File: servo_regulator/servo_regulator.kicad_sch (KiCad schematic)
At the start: 18 parts, among them J1 Conn_01x03_Socket, Q1 2N7002K

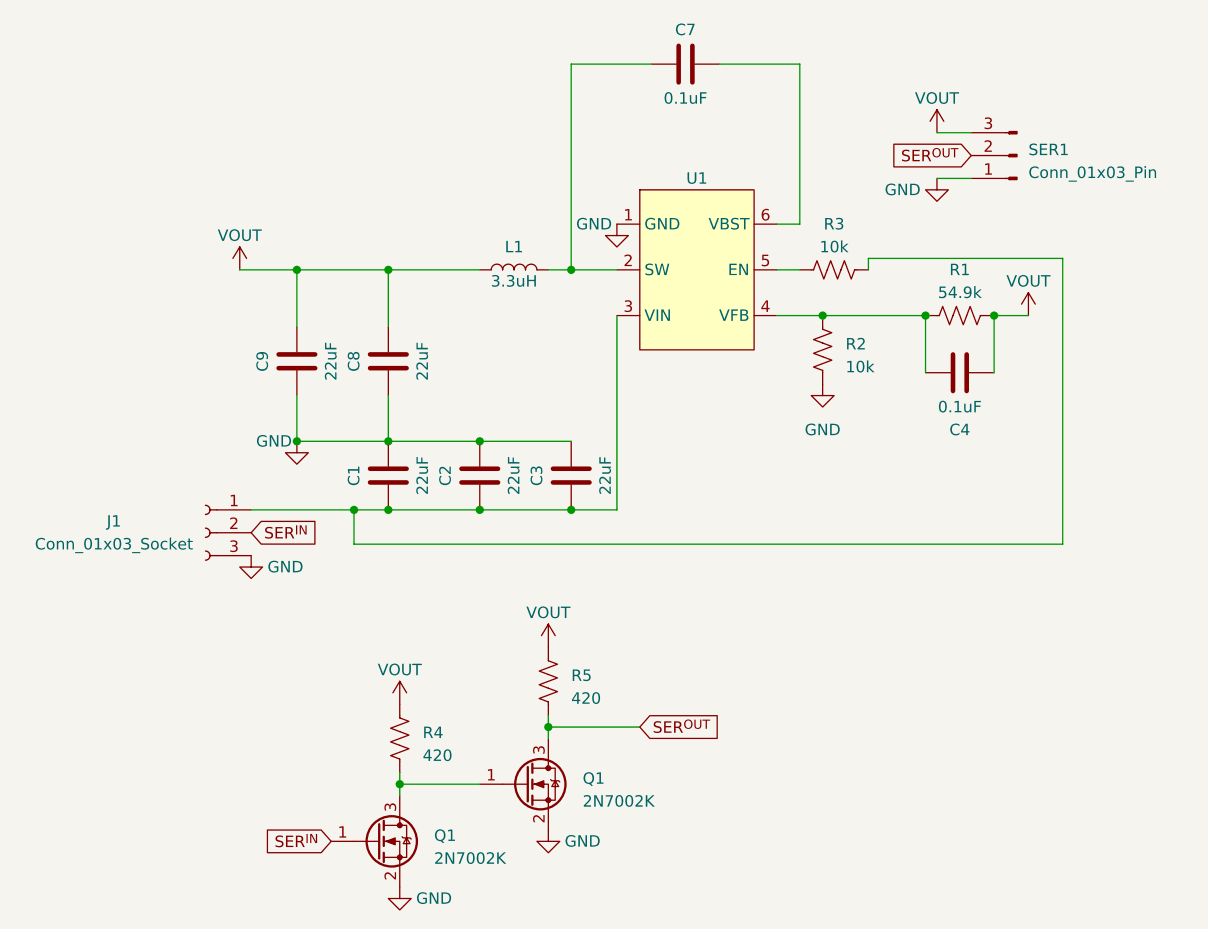
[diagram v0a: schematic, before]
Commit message: Updated spar sensor to reflect order
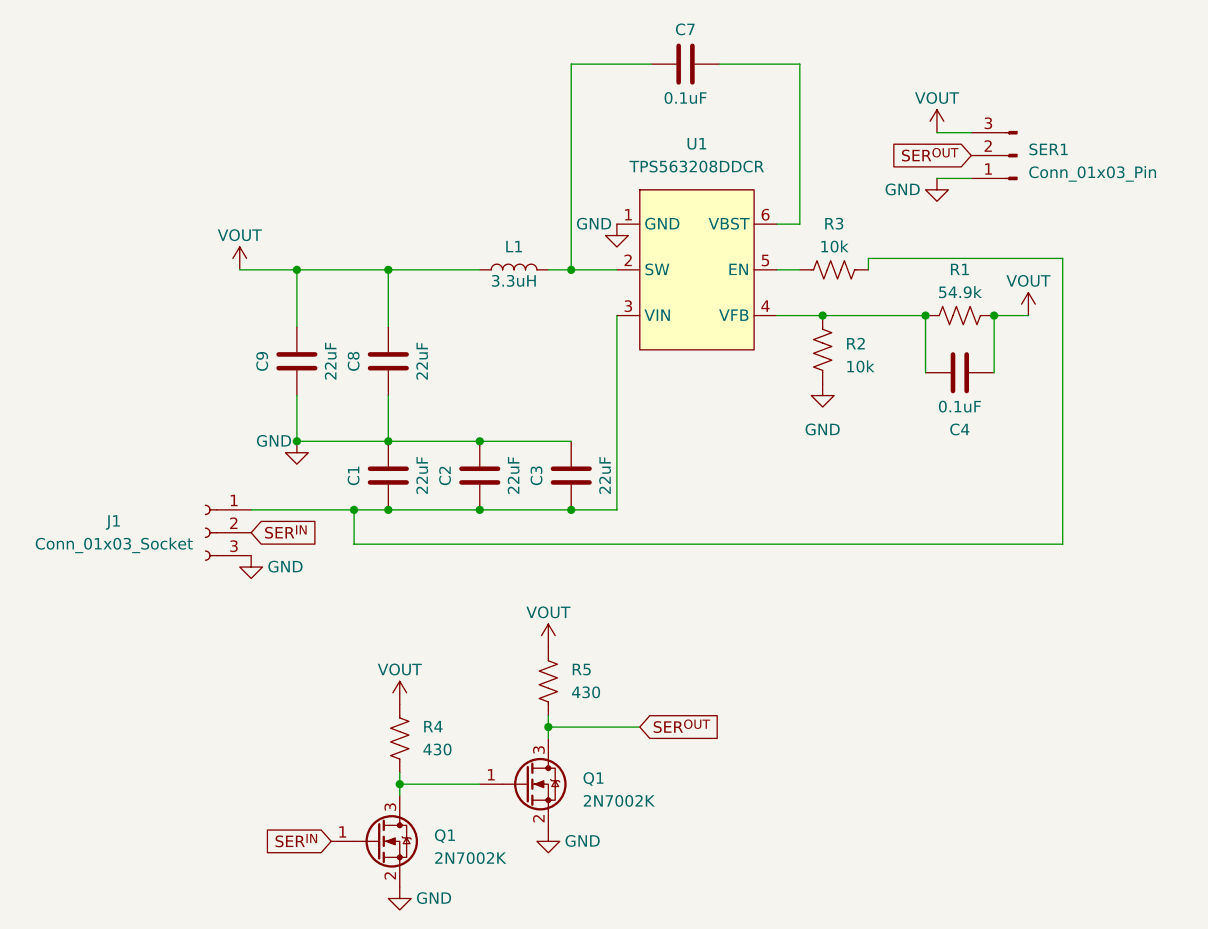
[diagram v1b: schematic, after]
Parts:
- R4, R5: value 420 -> 430
- U1: value ~ -> TPS563208DDCR
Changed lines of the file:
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@@
     (pin "2")
     (instances
-      (project "servoregulatorsv1"
+      (project "servo_regulator"
         (path "/73a2c705-23c6-4b38-b747-fa1f3c1277cb"
           (reference "R3") (unit 1)
@@
     (pin "1")
     (instances
-      (project "servoregulatorsv1"
+      (project "servo_regulator"
         (path "/73a2c705-23c6-4b38-b747-fa1f3c1277cb"
           (reference "#PWR01") (unit 1)
@@
     (pin "1")
     (instances
-      (project "servoregulatorsv1"
+      (project "servo_regulator"
         (path "/73a2c705-23c6-4b38-b747-fa1f3c1277cb"
           (reference "#PWR05") (unit 1)
@@
   (symbol (lib_id "Device:R_US") (at 125.73 137.16 0) (unit 1)
     (in_bom yes) (on_board yes) (dnp no) (fields_autoplaced)
-    (property "Reference" "R5" (at 128.27 136.525 0)
+    (property "Reference" "R5" (at 128.27 135.89 0)
       (effects (font (size 1.27 1.27)) (justify left))
     )
-    (property "Value" "420" (at 128.27 139.065 0)
+    (property "Value" "430" (at 128.27 138.43 0)
       (effects (font (size 1.27 1.27)) (justify left))
     )
@@
     (pin "2")
     (instances
-      (project "servoregulatorsv1"
+      (project "servo_regulator"
         (path "/73a2c705-23c6-4b38-b747-fa1f3c1277cb"
           (reference "R5") (unit 1)
@@
   (symbol (lib_id "Regulators:TPS563208DDCR") (at 142.24 91.44 0) (unit 1)
     (in_bom yes) (on_board yes) (dnp no) (fields_autoplaced)
-    (property "Reference" "U1" (at 142.24 81.28 0)
-      (effects (font (size 1.27 1.27)))
-    )
-    (property "Value" "~" (at 123.19 102.87 0)
+    (property "Reference" "U1" (at 142.24 77.47 0)
+      (effects (font (size 1.27 1.27)))
+    )
+    (property "Value" "TPS563208DDCR" (at 142.24 80.01 0)
       (effects (font (size 1.27 1.27)))
     )
@@
     (pin "6")
     (instances
-      (project "servoregulatorsv1"
+      (project "servo_regulator"
         (path "/73a2c705-23c6-4b38-b747-fa1f3c1277cb"
           (reference "U1") (unit 1)
@@
         )
       )
-      (project "servoregulatorsv1"
+      (project "servo_regulator"
         (path "/73a2c705-23c6-4b38-b747-fa1f3c1277cb"
           (reference "Q1") (unit 1)
@@
     (pin "1")
     (instances
-      (project "servoregulatorsv1"
+      (project "servo_regulator"
         (path "/73a2c705-23c6-4b38-b747-fa1f3c1277cb"
           (reference "#PWR07") (unit 1)
@@
     (pin "1")
     (instances
-      (project "servoregulatorsv1"
+      (project "servo_regulator"
         (path "/73a2c705-23c6-4b38-b747-fa1f3c1277cb"
           (reference "#PWR08") (unit 1)
@@
     (pin "2")
     (instances
-      (project "servoregulatorsv1"
+      (project "servo_regulator"
         (path "/73a2c705-23c6-4b38-b747-fa1f3c1277cb"
           (reference "C7") (unit 1)
@@
     (pin "2")
     (instances
-      (project "servoregulatorsv1"
+      (project "servo_regulator"
         (path "/73a2c705-23c6-4b38-b747-fa1f3c1277cb"
           (reference "L1") (unit 1)
@@
     (pin "1")
     (instances
-      (project "servoregulatorsv1"
+      (project "servo_regulator"
         (path "/73a2c705-23c6-4b38-b747-fa1f3c1277cb"
           (reference "#PWR09") (unit 1)
@@
     (pin "1")
     (instances
-      (project "servoregulatorsv1"
+      (project "servo_regulator"
         (path "/73a2c705-23c6-4b38-b747-fa1f3c1277cb"
           (reference "#PWR03") (unit 1)
@@
     (pin "1")
     (instances
-      (project "servoregulatorsv1"
+      (project "servo_regulator"
         (path "/73a2c705-23c6-4b38-b747-fa1f3c1277cb"
           (reference "#PWR011") (unit 1)
@@
     (pin "1")
     (instances
-      (project "servoregulatorsv1"
+      (project "servo_regulator"
         (path "/73a2c705-23c6-4b38-b747-fa1f3c1277cb"
           (reference "#PWR010") (unit 1)
@@
     (pin "3")
     (instances
-      (project "servoregulatorsv1"
+      (project "servo_regulator"
         (path "/73a2c705-23c6-4b38-b747-fa1f3c1277cb"
           (reference "SER1") (unit 1)
@@
     (pin "2")
     (instances
-      (project "servoregulatorsv1"
+      (project "servo_regulator"
         (path "/73a2c705-23c6-4b38-b747-fa1f3c1277cb"
           (reference "C3") (unit 1)
@@
     (pin "1")
     (instances
-      (project "servoregulatorsv1"
+      (project "servo_regulator"
         (path "/73a2c705-23c6-4b38-b747-fa1f3c1277cb"
           (reference "#PWR06") (unit 1)
@@
     (pin "1")
     (instances
-      (project "servoregulatorsv1"
+      (project "servo_regulator"
         (path "/73a2c705-23c6-4b38-b747-fa1f3c1277cb"
           (reference "#PWR04") (unit 1)
@@
     (pin "2")
     (instances
-      (project "servoregulatorsv1"
+      (project "servo_regulator"
         (path "/73a2c705-23c6-4b38-b747-fa1f3c1277cb"
           (reference "C9") (unit 1)
@@
     (pin "2")
     (instances
-      (project "servoregulatorsv1"
+      (project "servo_regulator"
         (path "/73a2c705-23c6-4b38-b747-fa1f3c1277cb"
           (reference "C8") (unit 1)
@@
     (pin "2")
     (instances
-      (project "servoregulatorsv1"
+      (project "servo_regulator"
         (path "/73a2c705-23c6-4b38-b747-fa1f3c1277cb"
           (reference "C4") (unit 1)
@@
     (pin "1")
     (instances
-      (project "servoregulatorsv1"
+      (project "servo_regulator"
         (path "/73a2c705-23c6-4b38-b747-fa1f3c1277cb"
           (reference "#PWR02") (unit 1)
@@
     (pin "2")
     (instances
-      (project "servoregulatorsv1"
+      (project "servo_regulator"
         (path "/73a2c705-23c6-4b38-b747-fa1f3c1277cb"
           (reference "C2") (unit 1)
@@
     (pin "3")
     (instances
-      (project "servoregulatorsv1"
+      (project "servo_regulator"
         (path "/73a2c705-23c6-4b38-b747-fa1f3c1277cb"
           (reference "J1") (unit 1)
@@
     (pin "2")
     (instances
-      (project "servoregulatorsv1"
+      (project "servo_regulator"
         (path "/73a2c705-23c6-4b38-b747-fa1f3c1277cb"
           (reference "R1") (unit 1)
@@
     (pin "2")
     (instances
-      (project "servoregulatorsv1"
+      (project "servo_regulator"
         (path "/73a2c705-23c6-4b38-b747-fa1f3c1277cb"
           (reference "C1") (unit 1)
@@
     (pin "1")
     (instances
-      (project "servoregulatorsv1"
+      (project "servo_regulator"
         (path "/73a2c705-23c6-4b38-b747-fa1f3c1277cb"
           (reference "#PWR012") (unit 1)
@@
         )
       )
-      (project "servoregulatorsv1"
+      (project "servo_regulator"
         (path "/73a2c705-23c6-4b38-b747-fa1f3c1277cb"
           (reference "Q2") (unit 1)
@@
   (symbol (lib_id "Device:R_US") (at 109.22 143.51 0) (unit 1)
     (in_bom yes) (on_board yes) (dnp no) (fields_autoplaced)
-    (property "Reference" "R4" (at 111.76 142.875 0)
+    (property "Reference" "R4" (at 111.76 142.24 0)
       (effects (font (size 1.27 1.27)) (justify left))
     )
-    (property "Value" "420" (at 111.76 145.415 0)
+    (property "Value" "430" (at 111.76 144.78 0)
       (effects (font (size 1.27 1.27)) (justify left))
     )
@@
     (pin "2")
     (instances
-      (project "servoregulatorsv1"
+      (project "servo_regulator"
         (path "/73a2c705-23c6-4b38-b747-fa1f3c1277cb"
           (reference "R4") (unit 1)
@@
     (pin "2")
     (instances
-      (project "servoregulatorsv1"
+      (project "servo_regulator"
         (path "/73a2c705-23c6-4b38-b747-fa1f3c1277cb"
           (reference "R2") (unit 1)

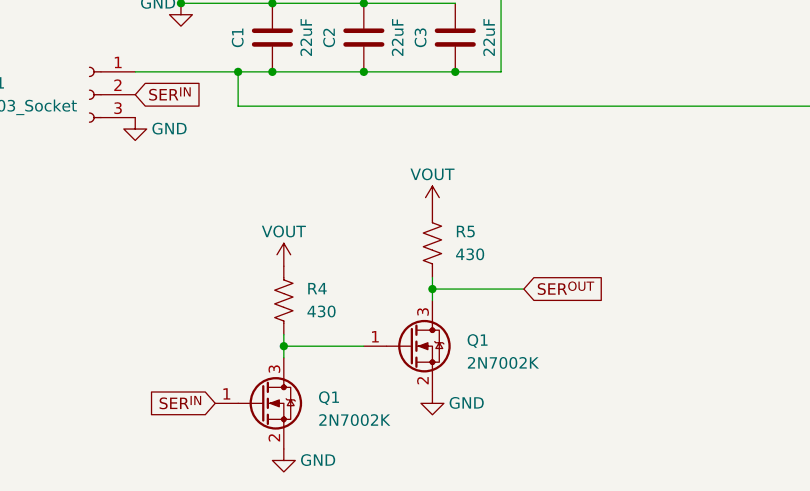
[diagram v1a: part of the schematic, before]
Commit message: Adjusted pullup resistors
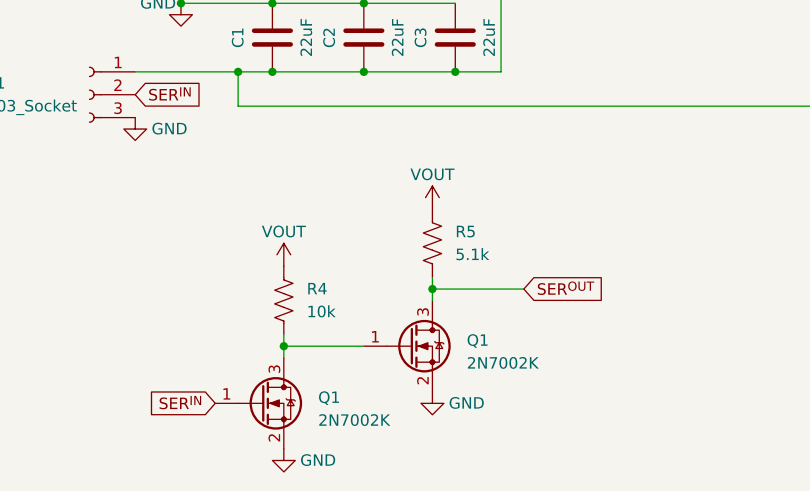
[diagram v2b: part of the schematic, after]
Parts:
- R4: value 430 -> 10k
- R5: value 430 -> 5.1k
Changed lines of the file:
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@@
       (effects (font (size 1.27 1.27)) (justify left))
     )
-    (property "Value" "430" (at 128.27 138.43 0)
+    (property "Value" "5.1k" (at 128.27 138.43 0)
       (effects (font (size 1.27 1.27)) (justify left))
     )
@@
       (effects (font (size 1.27 1.27)) (justify left))
     )
-    (property "Value" "430" (at 111.76 144.78 0)
-      (effects (font (size 1.27 1.27)) (justify left))
-    )
+    (property "Value" "10k" (at 111.76 144.78 0)
+      (effects (font (size 1.27 1.27)) (justify left))
+    )
